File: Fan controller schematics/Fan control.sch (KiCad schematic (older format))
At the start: 20 parts, among them Q1 SI2302, Q2 SI2302, Q3 SI2302, Q4 SI2302, Q5 SI2302

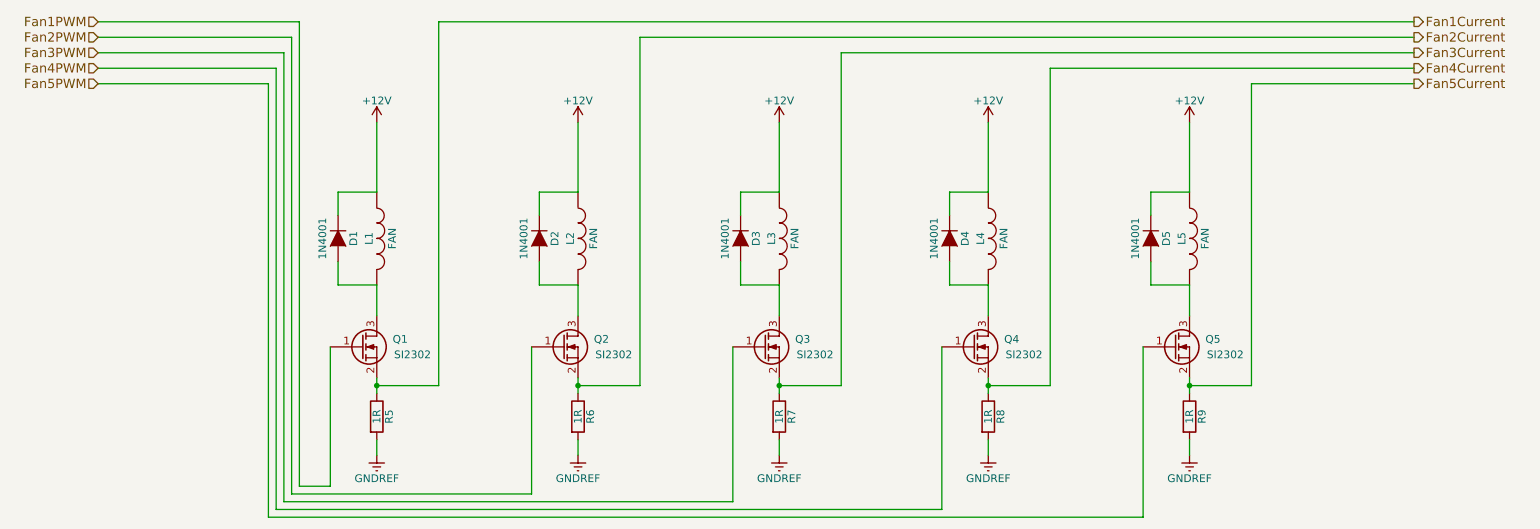
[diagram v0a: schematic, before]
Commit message: Add ADC filter and ref
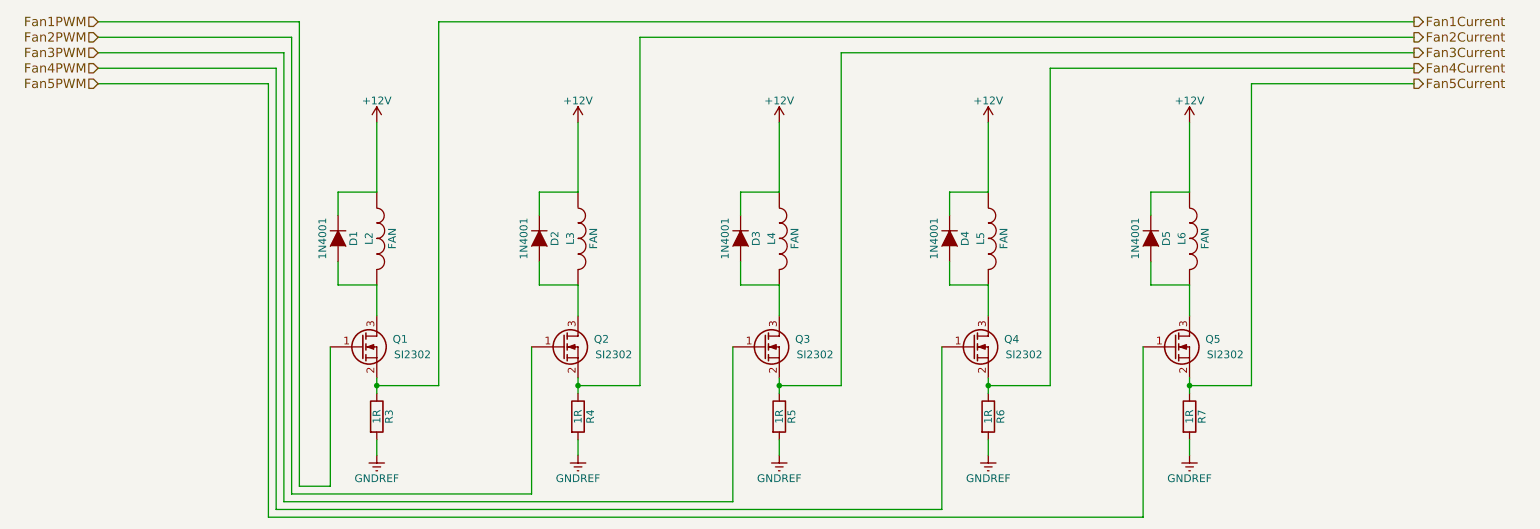
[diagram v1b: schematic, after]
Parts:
- renumbered L1 to L2, L2 to L3, L3 to L4, L4 to L5, L5 to L6, R5 to R3, R6 to R4, R7 to R5, R8 to R6, R9 to R7
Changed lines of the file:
@@
 $EndComp
 $Comp
-L INDUCTOR L5
+L INDUCTOR L6
 U 1 1 57D81757
 P 8750 4100
-F 0 "L5" V 8700 4100 50  0000 C CNN
+F 0 "L6" V 8700 4100 50  0000 C CNN
 F 1 "FAN" V 8850 4100 50  0000 C CNN
 F 2 "" H 8750 4100 50  0000 C CNN
@@
 	8750 4400 8750 4600
 $Comp
-L GNDREF #PWR18
+L GNDREF #PWR17
 U 1 1 57D81770
 P 8750 5500
-F 0 "#PWR18" H 8750 5250 50  0001 C CNN
+F 0 "#PWR17" H 8750 5250 50  0001 C CNN
 F 1 "GNDREF" H 8750 5350 50  0000 C CNN
 F 2 "" H 8750 5500 50  0000 C CNN
@@
 	8750 3800 8750 3350
 $Comp
-L +12V #PWR17
+L +12V #PWR16
 U 1 1 57D8178A
 P 8750 3350
-F 0 "#PWR17" H 8750 3200 50  0001 C CNN
+F 0 "#PWR16" H 8750 3200 50  0001 C CNN
 F 1 "+12V" H 8750 3490 50  0000 C CNN
 F 2 "" H 8750 3350 50  0000 C CNN
@@
 $EndComp
 $Comp
-L INDUCTOR L4
+L INDUCTOR L5
 U 1 1 57D817A4
 P 7450 4100
-F 0 "L4" V 7400 4100 50  0000 C CNN
+F 0 "L5" V 7400 4100 50  0000 C CNN
 F 1 "FAN" V 7550 4100 50  0000 C CNN
 F 2 "" H 7450 4100 50  0000 C CNN
@@
 	7450 4400 7450 4600
 $Comp
-L GNDREF #PWR16
+L GNDREF #PWR15
 U 1 1 57D817BD
 P 7450 5500
-F 0 "#PWR16" H 7450 5250 50  0001 C CNN
+F 0 "#PWR15" H 7450 5250 50  0001 C CNN
 F 1 "GNDREF" H 7450 5350 50  0000 C CNN
 F 2 "" H 7450 5500 50  0000 C CNN
@@
 	7450 3800 7450 3350
 $Comp
-L +12V #PWR15
+L +12V #PWR14
 U 1 1 57D817D7
 P 7450 3350
-F 0 "#PWR15" H 7450 3200 50  0001 C CNN
+F 0 "#PWR14" H 7450 3200 50  0001 C CNN
 F 1 "+12V" H 7450 3490 50  0000 C CNN
 F 2 "" H 7450 3350 50  0000 C CNN
@@
 $EndComp
 $Comp
-L INDUCTOR L3
+L INDUCTOR L4
 U 1 1 57D817F1
 P 6100 4100
-F 0 "L3" V 6050 4100 50  0000 C CNN
+F 0 "L4" V 6050 4100 50  0000 C CNN
 F 1 "FAN" V 6200 4100 50  0000 C CNN
 F 2 "" H 6100 4100 50  0000 C CNN
@@
 $EndComp
 $Comp
-L GNDREF #PWR14
+L GNDREF #PWR13
 U 1 1 57D8180A
 P 6100 5500
-F 0 "#PWR14" H 6100 5250 50  0001 C CNN
+F 0 "#PWR13" H 6100 5250 50  0001 C CNN
 F 1 "GNDREF" H 6100 5350 50  0000 C CNN
 F 2 "" H 6100 5500 50  0000 C CNN
@@
 	6100 3800 6100 3350
 $Comp
-L +12V #PWR13
+L +12V #PWR12
 U 1 1 57D81824
 P 6100 3350
-F 0 "#PWR13" H 6100 3200 50  0001 C CNN
+F 0 "#PWR12" H 6100 3200 50  0001 C CNN
 F 1 "+12V" H 6100 3490 50  0000 C CNN
 F 2 "" H 6100 3350 50  0000 C CNN
@@
 $EndComp
 $Comp
-L INDUCTOR L2
+L INDUCTOR L3
 U 1 1 57D8183E
 P 4800 4100
-F 0 "L2" V 4750 4100 50  0000 C CNN
+F 0 "L3" V 4750 4100 50  0000 C CNN
 F 1 "FAN" V 4900 4100 50  0000 C CNN
 F 2 "" H 4800 4100 50  0000 C CNN
@@
 	4800 4400 4800 4600
 $Comp
-L GNDREF #PWR12
+L GNDREF #PWR11
 U 1 1 57D81857
 P 4800 5500
-F 0 "#PWR12" H 4800 5250 50  0001 C CNN
+F 0 "#PWR11" H 4800 5250 50  0001 C CNN
 F 1 "GNDREF" H 4800 5350 50  0000 C CNN
 F 2 "" H 4800 5500 50  0000 C CNN
@@
 	4800 3800 4800 3350
 $Comp
-L +12V #PWR11
+L +12V #PWR10
 U 1 1 57D81871
 P 4800 3350
-F 0 "#PWR11" H 4800 3200 50  0001 C CNN
+F 0 "#PWR10" H 4800 3200 50  0001 C CNN
 F 1 "+12V" H 4800 3490 50  0000 C CNN
 F 2 "" H 4800 3350 50  0000 C CNN
@@
 $EndComp
 $Comp
-L INDUCTOR L1
+L INDUCTOR L2
 U 1 1 57D8188B
 P 3500 4100
-F 0 "L1" V 3450 4100 50  0000 C CNN
+F 0 "L2" V 3450 4100 50  0000 C CNN
 F 1 "FAN" V 3600 4100 50  0000 C CNN
 F 2 "" H 3500 4100 50  0000 C CNN
@@
 	3500 4400 3500 4600
 $Comp
-L GNDREF #PWR10
+L GNDREF #PWR9
 U 1 1 57D818A4
 P 3500 5500
-F 0 "#PWR10" H 3500 5250 50  0001 C CNN
+F 0 "#PWR9" H 3500 5250 50  0001 C CNN
 F 1 "GNDREF" H 3500 5350 50  0000 C CNN
 F 2 "" H 3500 5500 50  0000 C CNN
@@
 	3500 3800 3500 3350
 $Comp
-L +12V #PWR9
+L +12V #PWR8
 U 1 1 57D818BE
 P 3500 3350
-F 0 "#PWR9" H 3500 3200 50  0001 C CNN
+F 0 "#PWR8" H 3500 3200 50  0001 C CNN
 F 1 "+12V" H 3500 3490 50  0000 C CNN
 F 2 "" H 3500 3350 50  0000 C CNN
@@
 	6100 4400 6100 4600
 $Comp
-L R R5
+L R R3
 U 1 1 57D833AB
 P 3500 5250
-F 0 "R5" V 3580 5250 50  0000 C CNN
+F 0 "R3" V 3580 5250 50  0000 C CNN
 F 1 "1R" V 3500 5250 50  0000 C CNN
 F 2 "" V 3430 5250 50  0000 C CNN
@@
 $EndComp
 Wire Wire Line
-	3500 5000 3500 5050
-Wire Wire Line
-	3500 5050 3500 5100
+	3500 5000 3500 5100
 Wire Wire Line
 	3500 5400 3500 5500
 $Comp
-L R R6
+L R R4
 U 1 1 57D83D2A
 P 4800 5250
-F 0 "R6" V 4880 5250 50  0000 C CNN
+F 0 "R4" V 4880 5250 50  0000 C CNN
 F 1 "1R" V 4800 5250 50  0000 C CNN
 F 2 "" V 4730 5250 50  0000 C CNN
@@
 $EndComp
 Wire Wire Line
-	4800 5000 4800 5050
-Wire Wire Line
-	4800 5050 4800 5100
+	4800 5000 4800 5100
 Wire Wire Line
 	4800 5400 4800 5500
 $Comp
-L R R7
+L R R5
 U 1 1 57D83D7D
 P 6100 5250
-F 0 "R7" V 6180 5250 50  0000 C CNN
+F 0 "R5" V 6180 5250 50  0000 C CNN
 F 1 "1R" V 6100 5250 50  0000 C CNN
 F 2 "" V 6030 5250 50  0000 C CNN
@@
 $EndComp
 Wire Wire Line
-	6100 5000 6100 5050
-Wire Wire Line
-	6100 5050 6100 5100
+	6100 5000 6100 5100
 Wire Wire Line
 	6100 5400 6100 5500
 $Comp
-L R R9
+L R R7
 U 1 1 57D83DD0
 P 8750 5250
-F 0 "R9" V 8830 5250 50  0000 C CNN
+F 0 "R7" V 8830 5250 50  0000 C CNN
 F 1 "1R" V 8750 5250 50  0000 C CNN
 F 2 "" V 8680 5250 50  0000 C CNN
@@
 $EndComp
 Wire Wire Line
-	8750 5000 8750 5050
-Wire Wire Line
-	8750 5050 8750 5100
+	8750 5000 8750 5100
 Wire Wire Line
 	8750 5400 8750 5500
 $Comp
-L R R8
+L R R6
 U 1 1 57D83F1D
 P 7450 5250
-F 0 "R8" V 7530 5250 50  0000 C CNN
+F 0 "R6" V 7530 5250 50  0000 C CNN
 F 1 "1R" V 7450 5250 50  0000 C CNN
 F 2 "" V 7380 5250 50  0000 C CNN
@@
 $EndComp
 Wire Wire Line
-	7450 5000 7450 5050
-Wire Wire Line
-	7450 5050 7450 5100
+	7450 5000 7450 5100
 Wire Wire Line
 	7450 5400 7450 5500

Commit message: Update schematic to v1.3
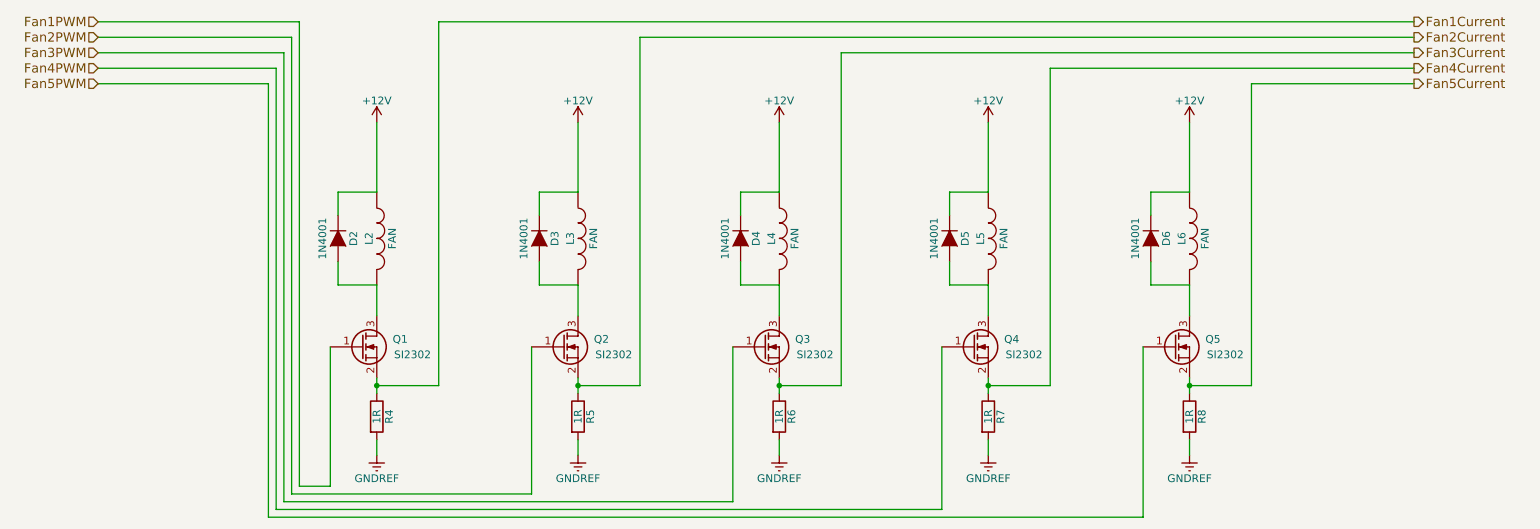
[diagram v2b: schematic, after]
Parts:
- renumbered D1 to D2, D2 to D3, D3 to D4, D4 to D5, D5 to D6, R3 to R4, R4 to R5, R5 to R6, R6 to R7, R7 to R8
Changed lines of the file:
@@
 	8750 4400 8750 4600
 $Comp
-L GNDREF #PWR17
+L GNDREF #PWR08
 U 1 1 57D81770
 P 8750 5500
-F 0 "#PWR17" H 8750 5250 50  0001 C CNN
+F 0 "#PWR08" H 8750 5250 50  0001 C CNN
 F 1 "GNDREF" H 8750 5350 50  0000 C CNN
 F 2 "" H 8750 5500 50  0000 C CNN
@@
 $EndComp
 $Comp
-L D D5
+L D D6
 U 1 1 57D81778
 P 8500 4100
-F 0 "D5" H 8500 4200 50  0000 C CNN
+F 0 "D6" H 8500 4200 50  0000 C CNN
 F 1 "1N4001" H 8500 4000 50  0000 C CNN
 F 2 "" H 8500 4100 50  0000 C CNN
@@
 	8750 3800 8750 3350
 $Comp
-L +12V #PWR16
+L +12V #PWR09
 U 1 1 57D8178A
 P 8750 3350
-F 0 "#PWR16" H 8750 3200 50  0001 C CNN
+F 0 "#PWR09" H 8750 3200 50  0001 C CNN
 F 1 "+12V" H 8750 3490 50  0000 C CNN
 F 2 "" H 8750 3350 50  0000 C CNN
@@
 	7450 4400 7450 4600
 $Comp
-L GNDREF #PWR15
+L GNDREF #PWR010
 U 1 1 57D817BD
 P 7450 5500
-F 0 "#PWR15" H 7450 5250 50  0001 C CNN
+F 0 "#PWR010" H 7450 5250 50  0001 C CNN
 F 1 "GNDREF" H 7450 5350 50  0000 C CNN
 F 2 "" H 7450 5500 50  0000 C CNN
@@
 $EndComp
 $Comp
-L D D4
+L D D5
 U 1 1 57D817C5
 P 7200 4100
-F 0 "D4" H 7200 4200 50  0000 C CNN
+F 0 "D5" H 7200 4200 50  0000 C CNN
 F 1 "1N4001" H 7200 4000 50  0000 C CNN
 F 2 "" H 7200 4100 50  0000 C CNN
@@
 	7450 3800 7450 3350
 $Comp
-L +12V #PWR14
+L +12V #PWR011
 U 1 1 57D817D7
 P 7450 3350
-F 0 "#PWR14" H 7450 3200 50  0001 C CNN
+F 0 "#PWR011" H 7450 3200 50  0001 C CNN
 F 1 "+12V" H 7450 3490 50  0000 C CNN
 F 2 "" H 7450 3350 50  0000 C CNN
@@
 $EndComp
 $Comp
-L GNDREF #PWR13
+L GNDREF #PWR012
 U 1 1 57D8180A
 P 6100 5500
-F 0 "#PWR13" H 6100 5250 50  0001 C CNN
+F 0 "#PWR012" H 6100 5250 50  0001 C CNN
 F 1 "GNDREF" H 6100 5350 50  0000 C CNN
 F 2 "" H 6100 5500 50  0000 C CNN
@@
 $EndComp
 $Comp
-L D D3
+L D D4
 U 1 1 57D81812
 P 5850 4100
-F 0 "D3" H 5850 4200 50  0000 C CNN
+F 0 "D4" H 5850 4200 50  0000 C CNN
 F 1 "1N4001" H 5850 4000 50  0000 C CNN
 F 2 "" H 5850 4100 50  0000 C CNN
@@
 	6100 3800 6100 3350
 $Comp
-L +12V #PWR12
+L +12V #PWR013
 U 1 1 57D81824
 P 6100 3350
-F 0 "#PWR12" H 6100 3200 50  0001 C CNN
+F 0 "#PWR013" H 6100 3200 50  0001 C CNN
 F 1 "+12V" H 6100 3490 50  0000 C CNN
 F 2 "" H 6100 3350 50  0000 C CNN
@@
 	4800 4400 4800 4600
 $Comp
-L GNDREF #PWR11
+L GNDREF #PWR014
 U 1 1 57D81857
 P 4800 5500
-F 0 "#PWR11" H 4800 5250 50  0001 C CNN
+F 0 "#PWR014" H 4800 5250 50  0001 C CNN
 F 1 "GNDREF" H 4800 5350 50  0000 C CNN
 F 2 "" H 4800 5500 50  0000 C CNN
@@
 $EndComp
 $Comp
-L D D2
+L D D3
 U 1 1 57D8185F
 P 4550 4100
-F 0 "D2" H 4550 4200 50  0000 C CNN
+F 0 "D3" H 4550 4200 50  0000 C CNN
 F 1 "1N4001" H 4550 4000 50  0000 C CNN
 F 2 "" H 4550 4100 50  0000 C CNN
@@
 	4800 3800 4800 3350
 $Comp
-L +12V #PWR10
+L +12V #PWR015
 U 1 1 57D81871
 P 4800 3350
-F 0 "#PWR10" H 4800 3200 50  0001 C CNN
+F 0 "#PWR015" H 4800 3200 50  0001 C CNN
 F 1 "+12V" H 4800 3490 50  0000 C CNN
 F 2 "" H 4800 3350 50  0000 C CNN
@@
 	3500 4400 3500 4600
 $Comp
-L GNDREF #PWR9
+L GNDREF #PWR016
 U 1 1 57D818A4
 P 3500 5500
-F 0 "#PWR9" H 3500 5250 50  0001 C CNN
+F 0 "#PWR016" H 3500 5250 50  0001 C CNN
 F 1 "GNDREF" H 3500 5350 50  0000 C CNN
 F 2 "" H 3500 5500 50  0000 C CNN
@@
 $EndComp
 $Comp
-L D D1
+L D D2
 U 1 1 57D818AC
 P 3250 4100
-F 0 "D1" H 3250 4200 50  0000 C CNN
+F 0 "D2" H 3250 4200 50  0000 C CNN
 F 1 "1N4001" H 3250 4000 50  0000 C CNN
 F 2 "" H 3250 4100 50  0000 C CNN
@@
 	3500 3800 3500 3350
 $Comp
-L +12V #PWR8
+L +12V #PWR017
 U 1 1 57D818BE
 P 3500 3350
-F 0 "#PWR8" H 3500 3200 50  0001 C CNN
+F 0 "#PWR017" H 3500 3200 50  0001 C CNN
 F 1 "+12V" H 3500 3490 50  0000 C CNN
 F 2 "" H 3500 3350 50  0000 C CNN
@@
 	6100 4400 6100 4600
 $Comp
-L R R3
+L R R4
 U 1 1 57D833AB
 P 3500 5250
-F 0 "R3" V 3580 5250 50  0000 C CNN
+F 0 "R4" V 3580 5250 50  0000 C CNN
 F 1 "1R" V 3500 5250 50  0000 C CNN
 F 2 "" V 3430 5250 50  0000 C CNN
@@
 	3500 5400 3500 5500
 $Comp
-L R R4
+L R R5
 U 1 1 57D83D2A
 P 4800 5250
-F 0 "R4" V 4880 5250 50  0000 C CNN
+F 0 "R5" V 4880 5250 50  0000 C CNN
 F 1 "1R" V 4800 5250 50  0000 C CNN
 F 2 "" V 4730 5250 50  0000 C CNN
@@
 	4800 5400 4800 5500
 $Comp
-L R R5
+L R R6
 U 1 1 57D83D7D
 P 6100 5250
-F 0 "R5" V 6180 5250 50  0000 C CNN
+F 0 "R6" V 6180 5250 50  0000 C CNN
 F 1 "1R" V 6100 5250 50  0000 C CNN
 F 2 "" V 6030 5250 50  0000 C CNN
@@
 	6100 5400 6100 5500
 $Comp
-L R R7
+L R R8
 U 1 1 57D83DD0
 P 8750 5250
-F 0 "R7" V 8830 5250 50  0000 C CNN
+F 0 "R8" V 8830 5250 50  0000 C CNN
 F 1 "1R" V 8750 5250 50  0000 C CNN
 F 2 "" V 8680 5250 50  0000 C CNN
@@
 	8750 5400 8750 5500
 $Comp
-L R R6
+L R R7
 U 1 1 57D83F1D
 P 7450 5250
-F 0 "R6" V 7530 5250 50  0000 C CNN
+F 0 "R7" V 7530 5250 50  0000 C CNN
 F 1 "1R" V 7450 5250 50  0000 C CNN
 F 2 "" V 7380 5250 50  0000 C CNN
